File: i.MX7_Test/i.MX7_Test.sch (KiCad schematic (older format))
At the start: 0 parts

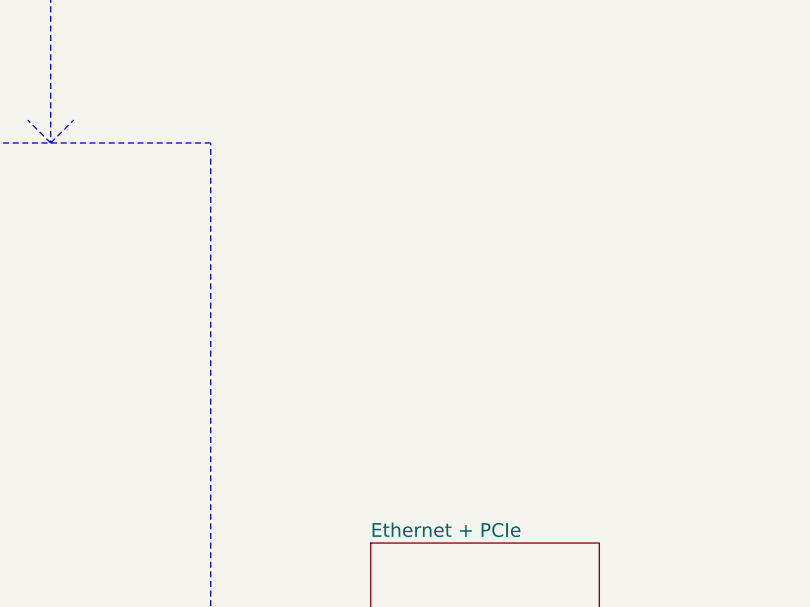
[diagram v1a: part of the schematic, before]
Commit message: Added some schematics for PMIC Added some Documentation for i.mx7
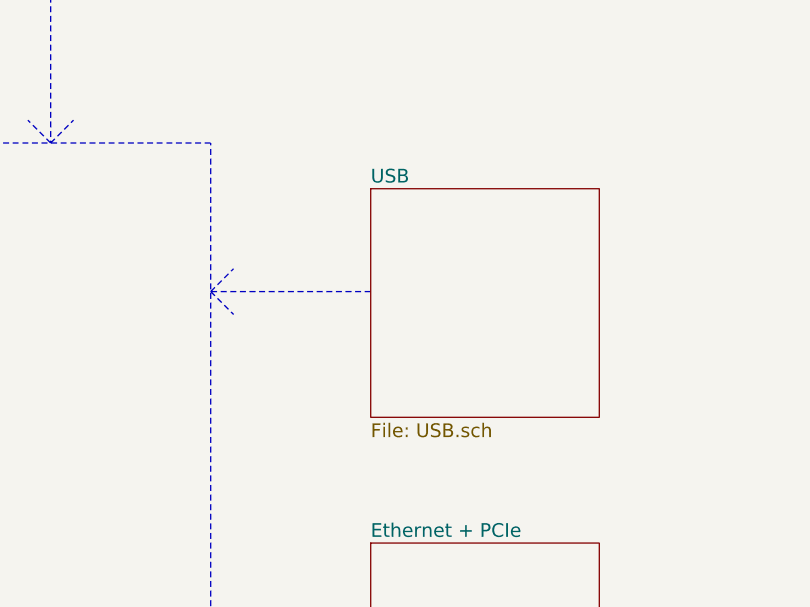
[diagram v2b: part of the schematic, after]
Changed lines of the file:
@@
 LIBS:contrib
 LIBS:valves
-LIBS:ACS
-LIBS:ADV7533
-LIBS:bluetooth
-LIBS:camera1
-LIBS:CC26XX
-LIBS:con-usb
-LIBS:ESP8266 - Kopie
-LIBS:ESP8266
-LIBS:ESS
-LIBS:LMH0030
-LIBS:lora
-LIBS:open-project
-LIBS:s_relays
-LIBS:shield_arduino
-LIBS:silego
-LIBS:siona
-LIBS:STM
-LIBS:stm8
-LIBS:stm32
-LIBS:TFP410
-LIBS:TI
-LIBS:top22xy
-LIBS:TRANSFORMER
-LIBS:USB_c
-LIBS:w_analog
-LIBS:w_connectors
-LIBS:w_device
-LIBS:w_logic
-LIBS:w_memory
-LIBS:w_microcontrollers
-LIBS:w_opto
-LIBS:w_relay
-LIBS:w_rtx
-LIBS:w_transistor
-LIBS:w_vacuum
-LIBS:IMX7D
-LIBS:voltages
-LIBS:pf3000
+LIBS:ip4292cz10-tbr
 LIBS:i.MX7_Test-cache
-EELAYER 25 0
+EELAYER 26 0
 EELAYER END
 $Descr A3 16535 11693
 encoding utf-8
-Sheet 1 10
+Sheet 1 11
 Title ""
 Date ""
@@
 Text Notes 11450 1400 0    60   ~ 0
 DCDC
+$Sheet
+S 8750 5250 1000 1000
+U 5926A8F7
+F0 "USB" 60
+F1 "USB.sch" 60
+$EndSheet
+Wire Notes Line
+	8750 5700 8050 5700
+Wire Notes Line
+	8050 5700 8150 5600
+Wire Notes Line
+	8050 5700 8150 5800
 $EndSCHEMATC
